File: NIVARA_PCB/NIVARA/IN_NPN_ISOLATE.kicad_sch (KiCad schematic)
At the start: 7 parts, among them U4 AT3H4A-CUH-S

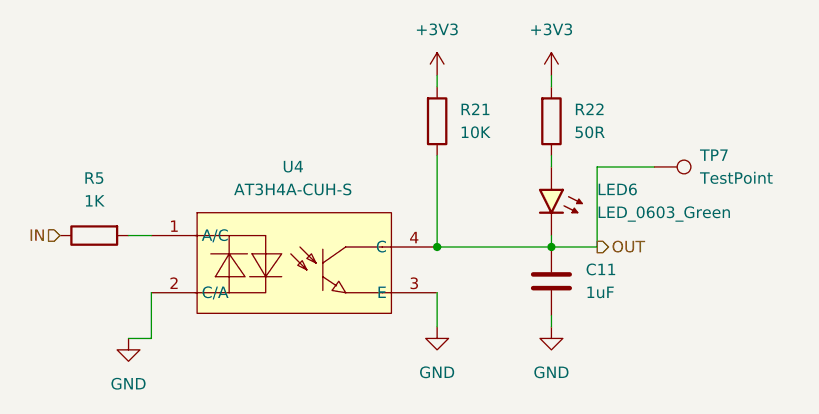
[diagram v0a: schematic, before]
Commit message: arreglo del desastre que tenia con las salidas PNP
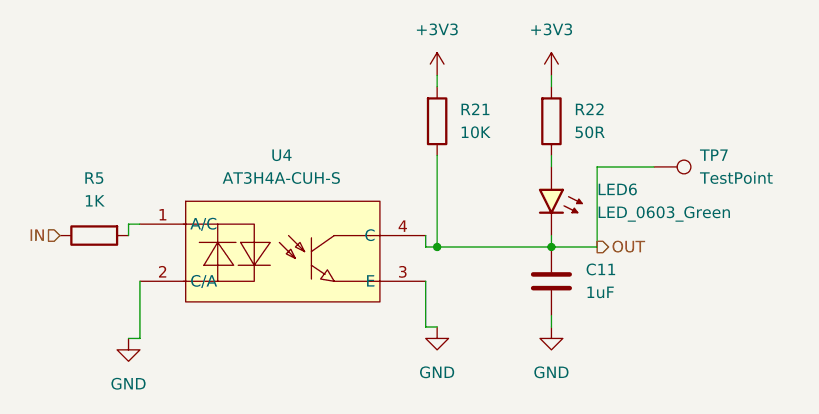
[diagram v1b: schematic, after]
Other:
- moved on the sheet: U4
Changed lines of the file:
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@@
 	(wire
 		(pts
-			(xy 102.87 104.14) (xy 105.41 104.14)
+			(xy 102.87 104.14) (xy 104.14 104.14)
 		)
 		(stroke
@@
 	(wire
 		(pts
+			(xy 135.89 102.87) (xy 137.16 102.87)
+		)
+		(stroke
+			(width 0)
+			(type default)
+		)
+	)
+	(wire
+		(pts
 			(xy 154.94 93.98) (xy 149.86 93.98)
 		)
@@
 	(wire
 		(pts
-			(xy 137.16 102.87) (xy 137.16 99.06)
-		)
-		(stroke
-			(width 0)
-			(type default)
-		)
-	)
-	(wire
-		(pts
-			(xy 105.41 104.14) (xy 105.41 99.06)
+			(xy 135.89 102.87) (xy 135.89 97.79)
+		)
+		(stroke
+			(width 0)
+			(type default)
+		)
+	)
+	(wire
+		(pts
+			(xy 135.89 93.98) (xy 137.16 93.98)
+		)
+		(stroke
+			(width 0)
+			(type default)
+		)
+	)
+	(wire
+		(pts
+			(xy 135.89 92.71) (xy 135.89 93.98)
+		)
+		(stroke
+			(width 0)
+			(type default)
+		)
+	)
+	(wire
+		(pts
+			(xy 102.87 91.44) (xy 102.87 92.71)
+		)
+		(stroke
+			(width 0)
+			(type default)
+		)
+	)
+	(wire
+		(pts
+			(xy 104.14 104.14) (xy 104.14 97.79)
 		)
 		(stroke
@@
 	(wire
 		(pts
-			(xy 102.87 92.71) (xy 105.41 92.71)
+			(xy 102.87 91.44) (xy 104.14 91.44)
 		)
 		(stroke
@@
 	(symbol
 		(lib_id "easyeda2kicad:AT3H4A-CUH-S")
-		(at 121.92 96.52 0)
+		(at 120.65 95.25 0)
 		(unit 1)
 		(exclude_from_sim no)
@@
 		(fields_autoplaced yes)
 		(property "Reference" "U4"
-			(at 121.16 85.09 0)
+			(at 119.89 83.82 0)
 			(effects
 				(font
@@
 		)
 		(property "Value" "AT3H4A-CUH-S"
-			(at 121.16 87.63 0)
+			(at 119.89 86.36 0)
 			(effects
 				(font
@@
 		)
 		(property "Footprint" "easyeda2kicad:SSOP-4_L2.7-W4.6-P1.27-LS7.0-TL"
-			(at 121.92 106.68 0)
+			(at 120.65 105.41 0)
 			(effects
 				(font
@@
 		)
 		(property "Datasheet" ""
-			(at 121.92 96.52 0)
+			(at 120.65 95.25 0)
 			(effects
 				(font
@@
 		)
 		(property "Description" ""
-			(at 121.92 96.52 0)
+			(at 120.65 95.25 0)
 			(effects
 				(font
@@
 		)
 		(property "LCSC Part" "C20612634"
-			(at 121.92 109.22 0)
+			(at 120.65 107.95 0)
 			(effects
 				(font
@@
 		)
 		(property "PART NUMBERT" "AT3H4A-CUH-S"
-			(at 121.92 96.52 0)
-			(effects
-				(font
+			(at 120.65 95.25 0)
+			(effects
+				(font
